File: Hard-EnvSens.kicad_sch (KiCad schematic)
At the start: 76 parts, among them J1 TYPE-C-31-M-12, J2 Conn_01x04_Socket, J3 Conn_02x02_Odd_Even, J4 Conn_01x04_Pin, J5 Conn_02x02_Odd_Even, J6 Conn_01x02_Pin, Q1 SS8050, Q2 SS8050, SW1 SW_Push, SW2 SW_Push, SW3 SW_Push, U1 LD1117S33TR_SOT223, U2 ESP32-C6-WROOM-1, U3 IP5306, U4 VEML7700-TR, U5 DPS368, U6 SGP41-D-R4, U7 SHT40-AD1B-R2, U8 AS7341-DLGT, U9 TPS79318DBVTG4

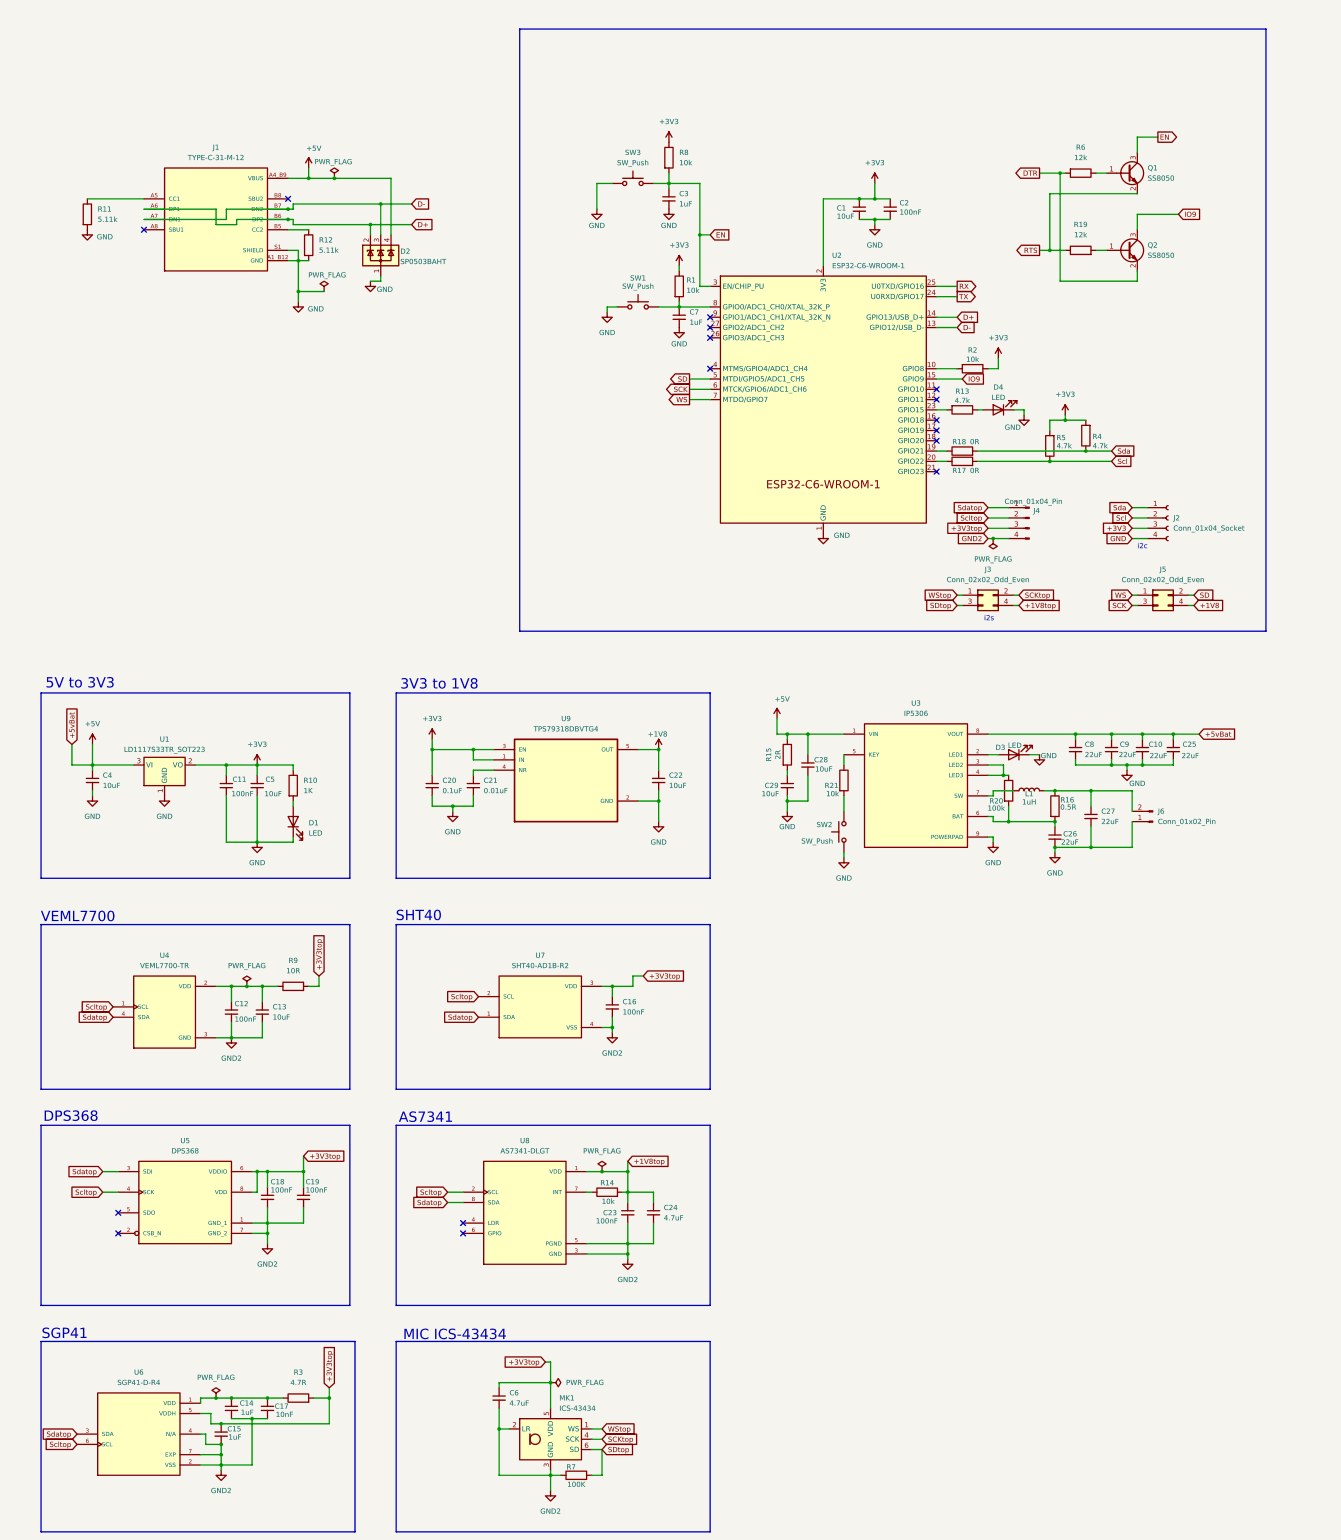
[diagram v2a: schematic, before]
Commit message: Correct commit for battery charger
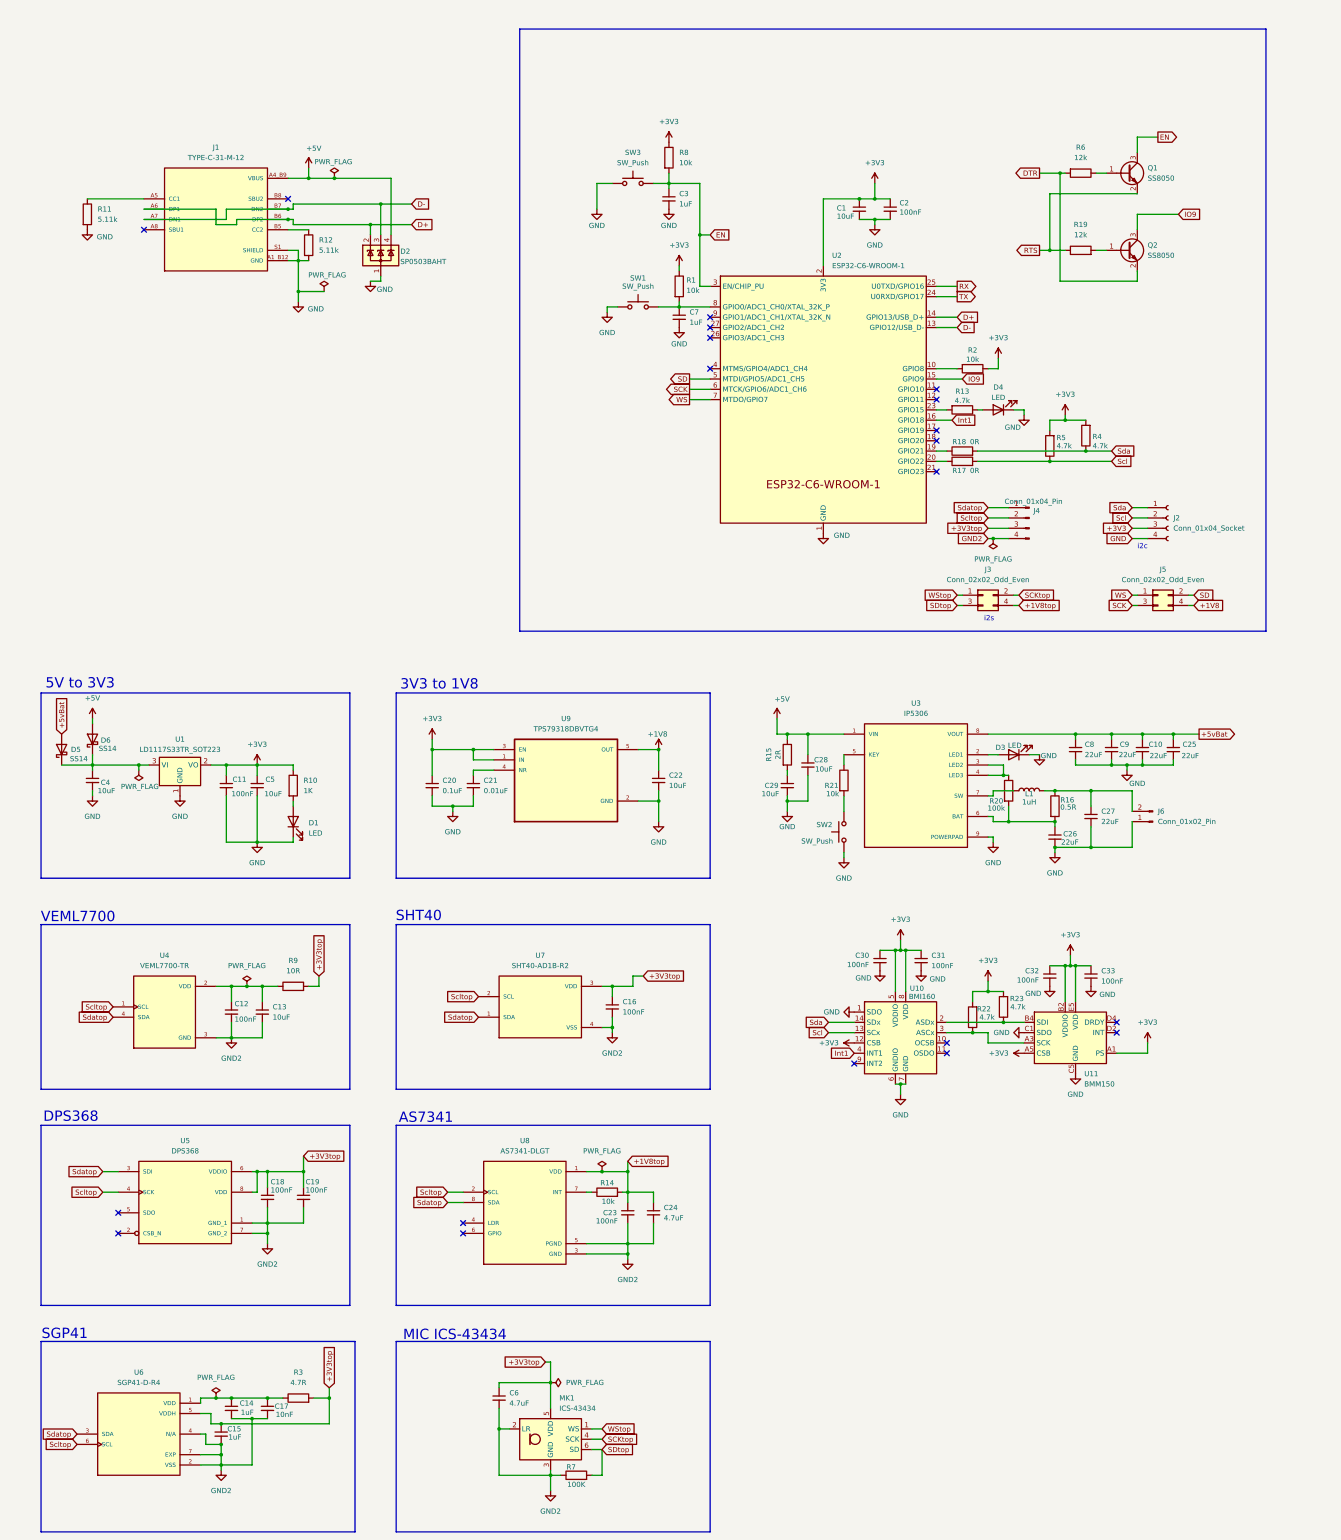
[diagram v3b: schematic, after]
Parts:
- added C30, C31, C32, C33: 100nF, Capacitor_SMD:C_0603_1608Metric, symbol Device:C_Small
- added D5, D6: SS14, Diode_SMD:D_SMA, symbol Diode:SS14
- added R22, R23: 4.7k, Resistor_SMD:R_0603_1608Metric, symbol Device:R
- added U10: BMI160, Package_LGA:Bosch_LGA-14_3x2.5mm_P0.5mm, symbol Sensor_Motion:BMI160
- added U11: BMM150, Package_CSP:WLCSP-12_1.56x1.56mm_P0.4mm, symbol Sensor_Magnetic:BMM150
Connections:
- net +3V3: now also C30.1, C31.1, C32.1, C33.1, R22.2, R23.2, U10.12 (CSB), U10.5 (VDDIO), U10.8 (VDD), U11.A1 (PS), U11.A5 (CSB), U11.B2 (VDDIO), U11.E5 (VDD)
- net +5V: now also D6.2 (A); no longer C10.1, C25.1, C4.1, C8.1, C9.1, U1.3 (VI), U3.8 (VOUT)
- net GND: now also C30.2, C31.2, C32.2, C33.2, U10.1 (SDO), U10.6 (GNDIO), U10.7 (GND), U11.C1 (SDO), U11.C5 (GND), U11.E1 (GND), U11.E3 (GND)
- net Scl: now also U10.13 (SCx)
- net Sda: now also U10.14 (SDx)
- net Int1: now reaches U2.16 (GPIO18)
- net Int1: now also U10.4 (INT1)
- new net: R23.1, U10.2 (ASDx), U11.B4 (SDI)
- new net: R22.1, U10.3 (ASCx), U11.A3 (SCK)
- new net: C4.1, D5.1 (K), D6.1 (K), U1.3 (VI)
- new net +5vBat: C10.1, C25.1, C8.1, C9.1, D5.2 (A), U3.8 (VOUT)
- no-connect marks 16 -> 20
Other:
- moved on the sheet: U1

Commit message: Improved whole board design
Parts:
- removed C33: 100nF, Capacitor_SMD:C_0603_1608Metric, symbol Device:C_Small
- removed R22, R23: 4.7k, Resistor_SMD:R_0603_1608Metric, symbol Device:R
- removed U11: BMM150, Package_CSP:WLCSP-12_1.56x1.56mm_P0.4mm, symbol Sensor_Magnetic:BMM150
- J1: footprint Biblioteca_Kicad:HRO_TYPE-C-31-M-12 -> libs:HRO_TYPE-C-31-M-12
- R13: value 4.7k -> 1k
- R21: value 10k -> 1k
- SW1, SW2, SW3: footprint Biblioteca_Kicad:SW_3-1437565-0 -> libs:Botao KH-6X6X5H-STM
- U2: footprint PCM_Espressif:ESP32-C6-WROOM-1 -> libs:XCVR_ESP32-C6-WROOM-1-N8
- U3: footprint libs:SOP127P600X165-9N -> IP5306:SOP127P600X165-9N
- U4: footprint Biblioteca_Kicad:XDCR_VEML7700-TR -> libs:XDCR_VEML7700-TR
- U6: footprint Biblioteca_Kicad:XDCR_SGP41-D-R4 -> libs:XDCR_SGP41-D-R4
- U7: footprint Biblioteca_Kicad:SHT4X -> libs:SHT4X
- renumbered R20 to R20*1
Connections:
- net +3V3: no longer C32.1
- net SCKtop: now also J3.3 (Pin_3); no longer J3.2 (Pin_2)
- net SDtop: now also J3.2 (Pin_2); no longer J3.3 (Pin_3)
- net at U3.5 (KEY): now also C32.1, SW2.2; no longer R21.1
- net at R21.2: now also C26.1, R16.2, R20*1.2, U3.6 (BAT); no longer SW2.2
- net at R20*1.1, U3.3 (LED2): no longer U3.4 (LED3)
- new net: R21.1, U3.4 (LED3)
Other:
- moved on the sheet: C28, C29, C30, C31, L1, R15, R20*1, U10

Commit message: Lot of improvements
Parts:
- J6: footprint Connector_PinHeader_2.54mm:PinHeader_1x02_P2.54mm_Vertical -> Connector_Molex:Molex_KK-254_AE-6410-02A_1x02_P2.54mm_Vertical
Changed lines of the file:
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@@
 			)
 		)
-		(property "Footprint" "Connector_PinHeader_2.54mm:PinHeader_1x02_P2.54mm_Vertical"
+		(property "Footprint" "Connector_Molex:Molex_KK-254_AE-6410-02A_1x02_P2.54mm_Vertical"
 			(at 298.45 218.44 0)
 			(effects

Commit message: Logos and corrections
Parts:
- added J7: Conn_01x04_Pin, Connector_PinHeader_2.54mm:PinHeader_1x04_P2.54mm_Vertical, symbol Connector:Conn_01x04_Pin
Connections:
- net +3V3: now also J7.4 (Pin_4)
- net GND: now also J7.2 (Pin_2)
- net Scl: now also J7.3 (Pin_3)
- net Sda: now also J7.1 (Pin_1)
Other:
- note added: "Extensao i2c"
- moved on the sheet: C30, C31, D2, J1, R11, R12, U10

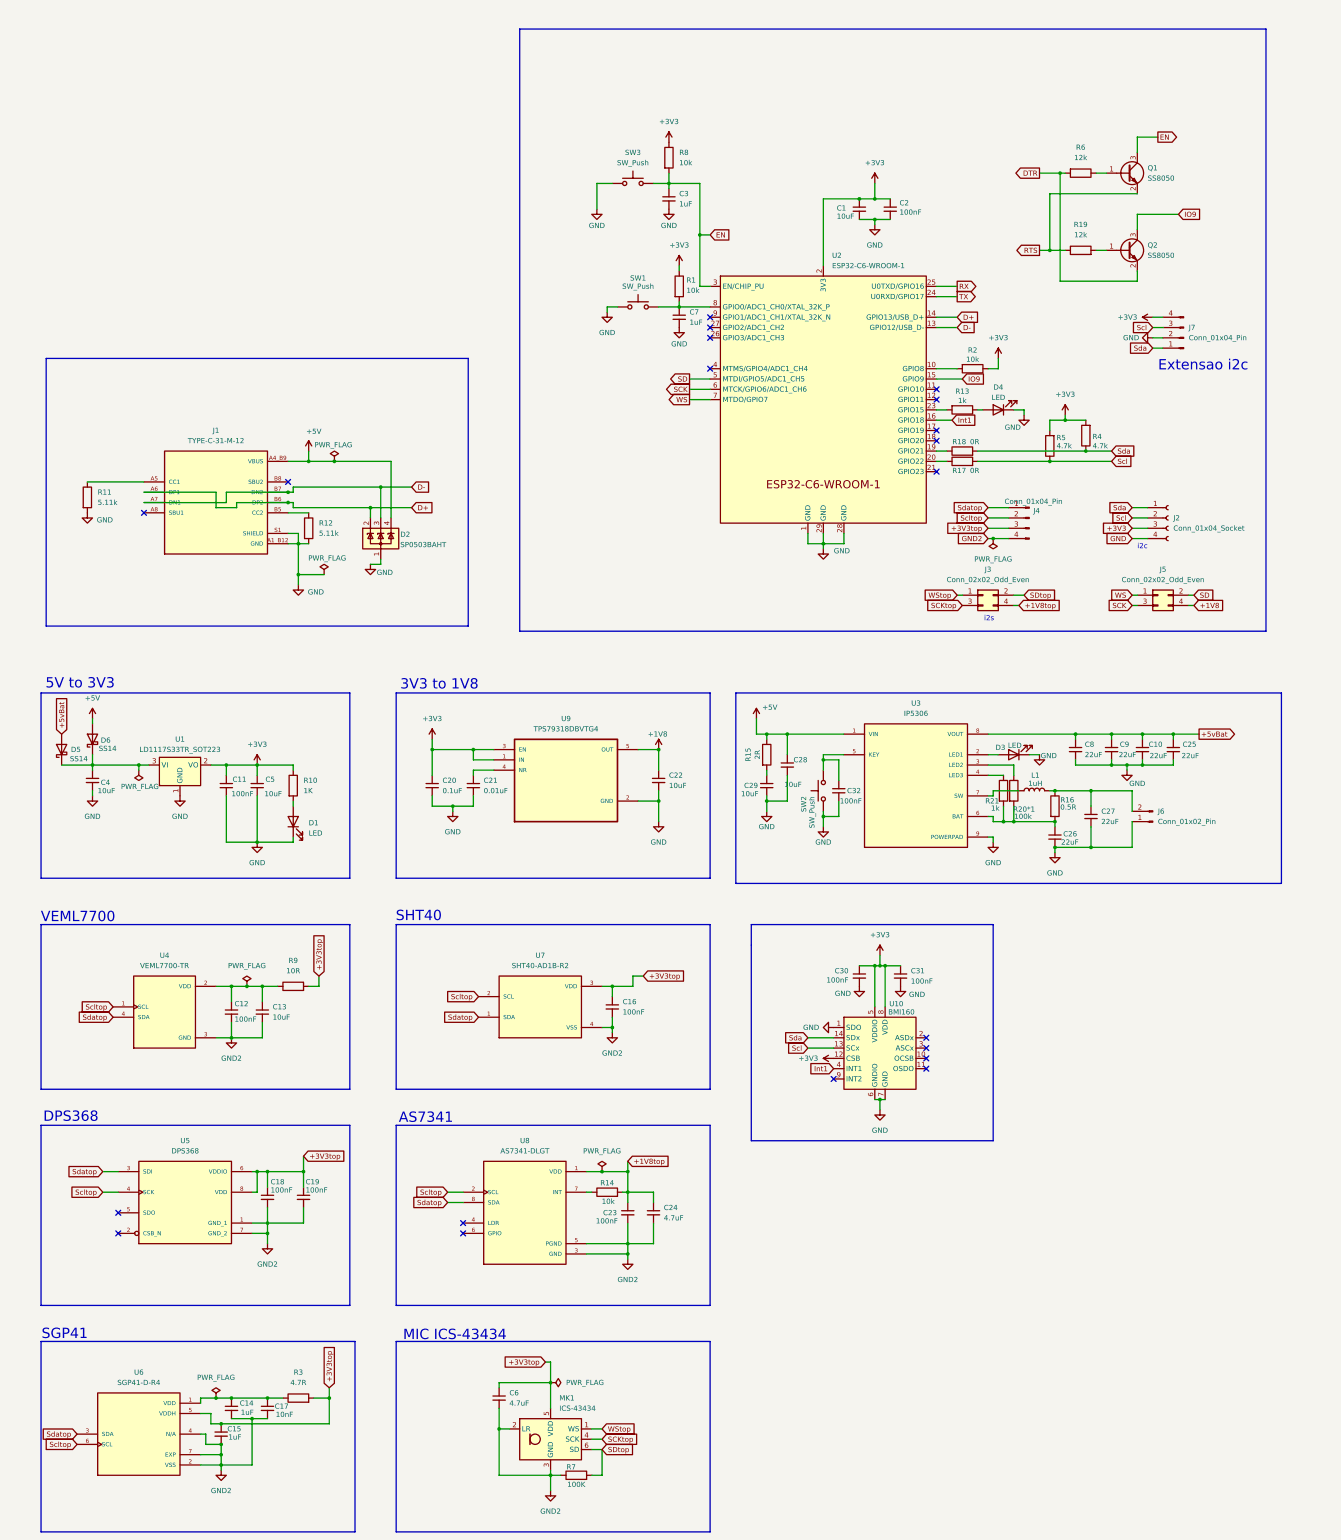
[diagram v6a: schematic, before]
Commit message: New charger + 3v3 Switch
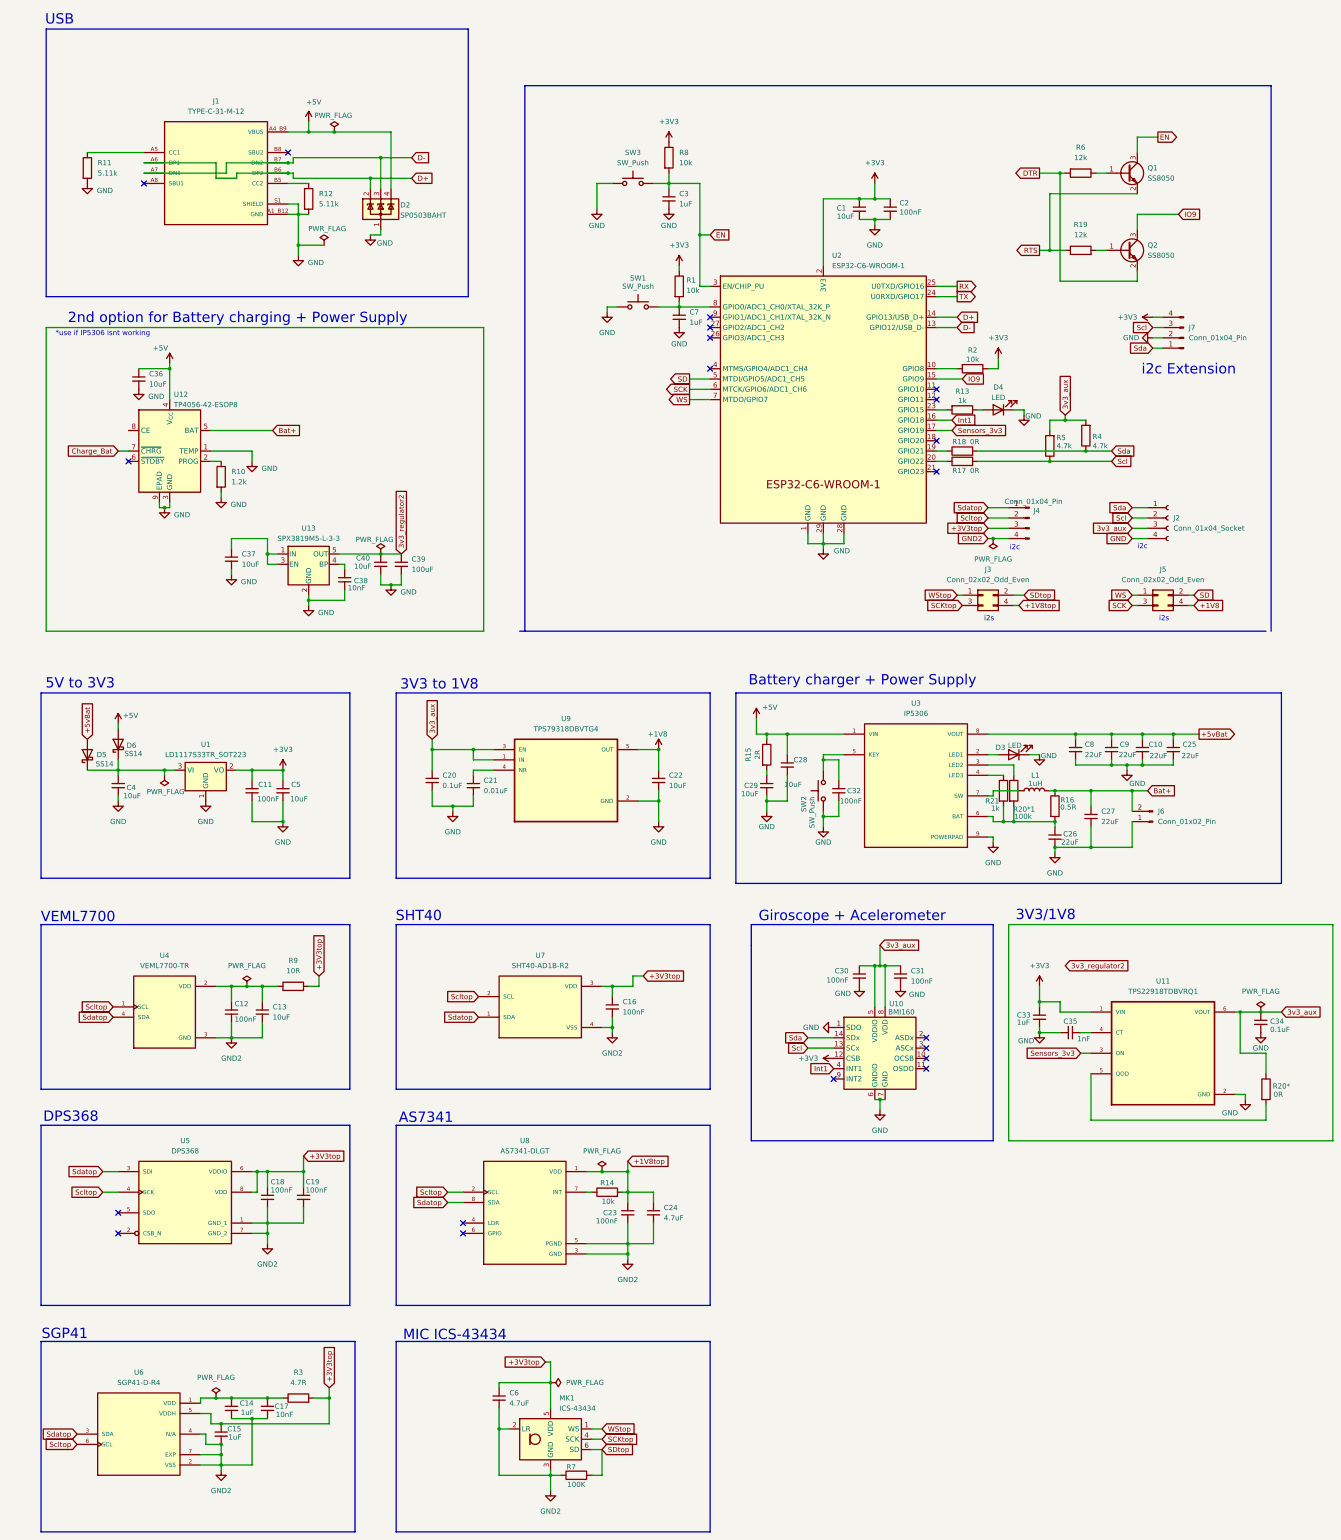
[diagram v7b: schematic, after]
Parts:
- removed D1: LED, LED_SMD:LED_0603_1608Metric, symbol Device:LED
- added C33: 1uF, Capacitor_SMD:C_0603_1608Metric, symbol Device:C_Small
- added C34: 0.1uF, Capacitor_SMD:C_0603_1608Metric, symbol Device:C_Small
- added C35: 1nF, Capacitor_SMD:C_0603_1608Metric, symbol Device:C_Small
- added C36, C37, C40: 10uF, Capacitor_SMD:C_0603_1608Metric, symbol Device:C_Small
- added C38: 10nF, Capacitor_SMD:C_0603_1608Metric, symbol Device:C_Small
- added C39: 100uF, Capacitor_SMD:C_0603_1608Metric, symbol Device:C_Small
- added R20*: 0R, Resistor_SMD:R_0603_1608Metric, symbol Device:R
- added U11: TPS22918TDBVRQ1, TPS22918TDBVRQ1:SOT95P280X145-6N, symbol TPS22918TDBVRQ1:TPS22918TDBVRQ1
- added U12: TP4056-42-ESOP8, Package_SO:SOIC-8-1EP_3.9x4.9mm_P1.27mm_EP2.41x3.3mm_ThermalVias, symbol Battery_Management:TP4056-42-ESOP8
- added U13: SPX3819M5-L-3-3, Package_TO_SOT_SMD:SOT-23-5, symbol Regulator_Linear:SPX3819M5-L-3-3
- R10: value 1K -> 1.2k
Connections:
- net +3V3: now also C33.1, U11.1 (VIN); no longer C20.1, C30.1, C31.1, J2.3 (Pin_3), R10.1, R4.2, R5.2, U10.5 (VDDIO), U10.8 (VDD), U9.1 (IN), U9.3 (EN)
- net +5V: now also C36.1, U12.4 (V_{CC})
- net GND: now also R10.2, C33.2, C34.2, C35.2, C36.2, C37.2, C38.2, C39.2, C40.2, U11.2 (GND), U12.1 (TEMP), U12.3 (GND), U12.9 (EPAD), U13.2 (GND)
- net Bat+: now reaches C27.1, J6.2 (Pin_2), L1.2, R16.1
- net Bat+: now also U12.5 (BAT)
- net Sensors_3v3: now reaches U2.17 (GPIO19)
- net Sensors_3v3: now also U11.3 (ON)
- new net: R10.1, U12.2 (PROG)
- new net: C37.1, U13.1 (IN), U13.3 (EN)
- new net: C38.1, U13.4 (BP)
- new net: C35.1, U11.4 (CT)
- new net: R20*.2, U11.5 (QOD)
- new net 3v3_aux: C20.1, C30.1, C31.1, C34.1, J2.3 (Pin_3), R20*.1, R4.2, R5.2, U10.5 (VDDIO), U10.8 (VDD), U11.6 (VOUT), U9.1 (IN), U9.3 (EN)
- new net 3v3_regulator2: C39.1, C40.1, U13.5 (OUT)
- new net Charge_Bat: U12.7 (~{CHRG})
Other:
- note added: "*use if IP5306 isnt working"
- note added: "2nd option for Battery charging + Power Supply"
- note added: "3V3/1V8"
- note added: "Battery charger + Power Supply"
- note added: "Giroscope + Acelerometer"
- note added: "USB"
- note added: "i2c Extension"
- note removed: "Extensao i2c"
- moved on the sheet: C11, C20, C4, C5, D2, D5, D6, J1, R11, R12, U1
